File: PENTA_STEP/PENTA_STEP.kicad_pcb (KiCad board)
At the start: 4 copper layers, 200 x 100 mm, 364 parts, among them J1 DB25_Female_LCNC, J10 ENC_HEADER, J11 ENC_HEADER, J12 PSoC_PROG, J13 PWR_SW_CH1, J14 SCREW TERM, J15 SCREW TERM, J16 ENC_HEADER, J17 ENC_HEADER, J18 SCREW TERM, J19 SCREW TERM, J2 MTA-100, J20 CYP_I2C, J21 PWR_SW_CH2, J3 USB_B, J4 SPARE_IN, J5 ENC_HEADER, J6 Conn_02x02_Odd_Even, J7 CYP_GPIO, J8 ICSP, J9 SCREW TERM, Q1 BUK9K45-100E,115, Q10 BUK9K45-100E,115, Q11 BUK9K45-100E,115, Q12 BUK9K45-100E,115, Q13 BUK9K45-100E,115, Q14 BUK9K45-100E,115, Q15 BUK9K45-100E,115, Q16 BUK9K45-100E,115, Q17 BUK9K45-100E,115, Q18 BUK9K45-100E,115, Q19 BUK9K45-100E,115, Q2 BUK9K45-100E,115, Q20 BUK9K45-100E,115, Q21 AON7804, Q3 BUK9K45-100E,115, Q4 BUK9K45-100E,115, Q5 BUK9K45-100E,115, Q6 BUK9K45-100E,115, Q7 BUK9K45-100E,115, Q8 BUK9K45-100E,115, Q9 BUK9K45-100E,115, U1 ATTINY841-SSU, U2 CY8C5468AXI-LP106, U3 TMC5160-TA, U4 TMC5160-TA, U5 TMC5160-TA, U6 TMC5160-TA, U7 TMC5160-TA, Y1 10MHz

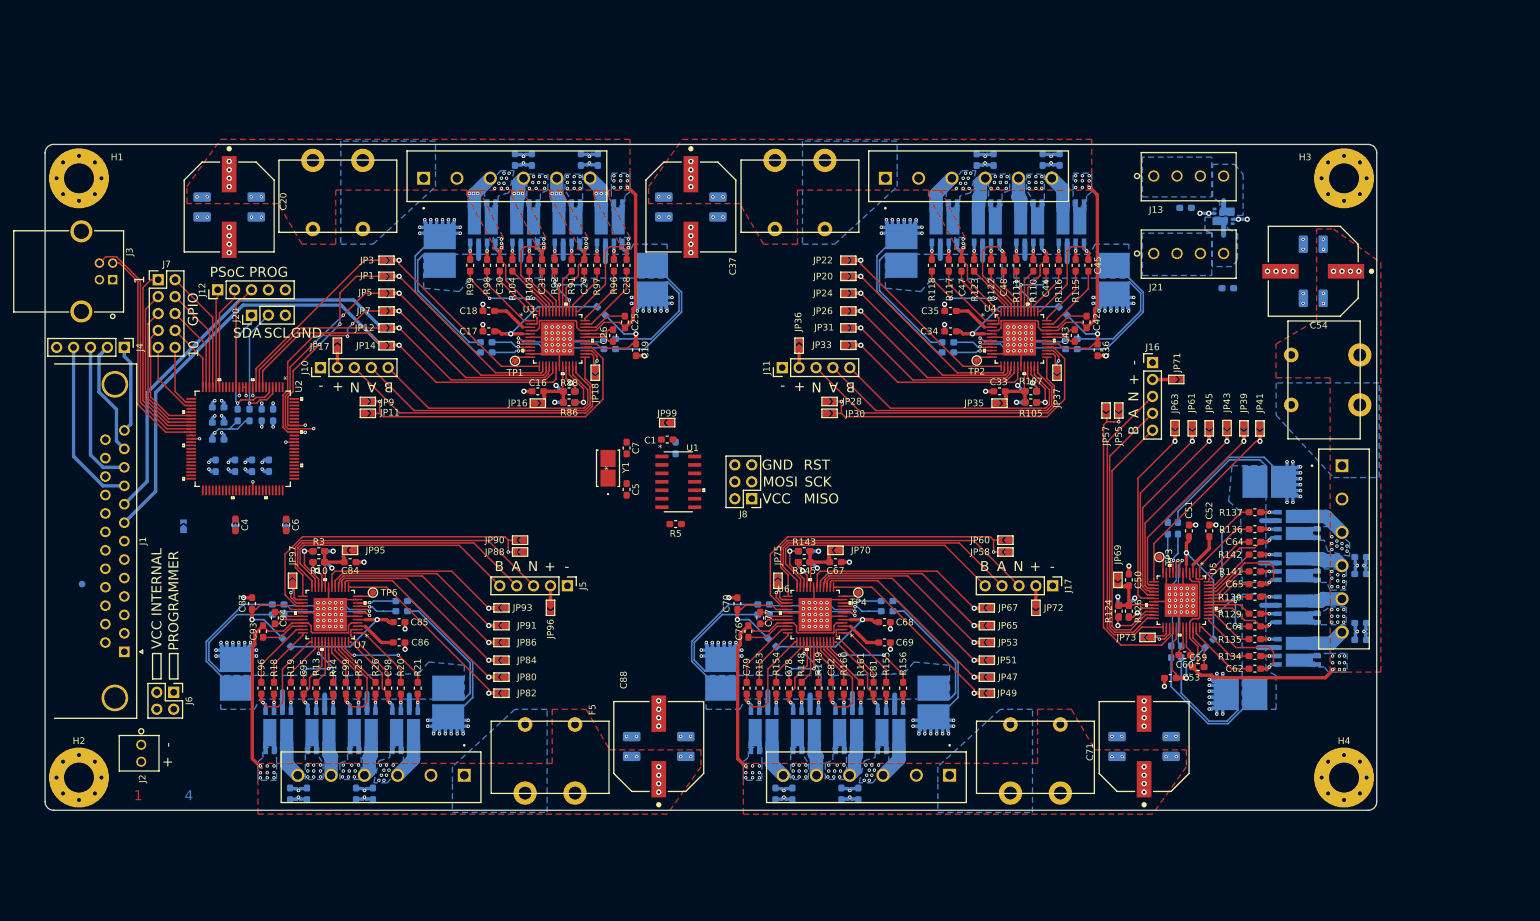
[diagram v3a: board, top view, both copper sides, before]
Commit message: majority routed, eliminated ATTINY coprocessor
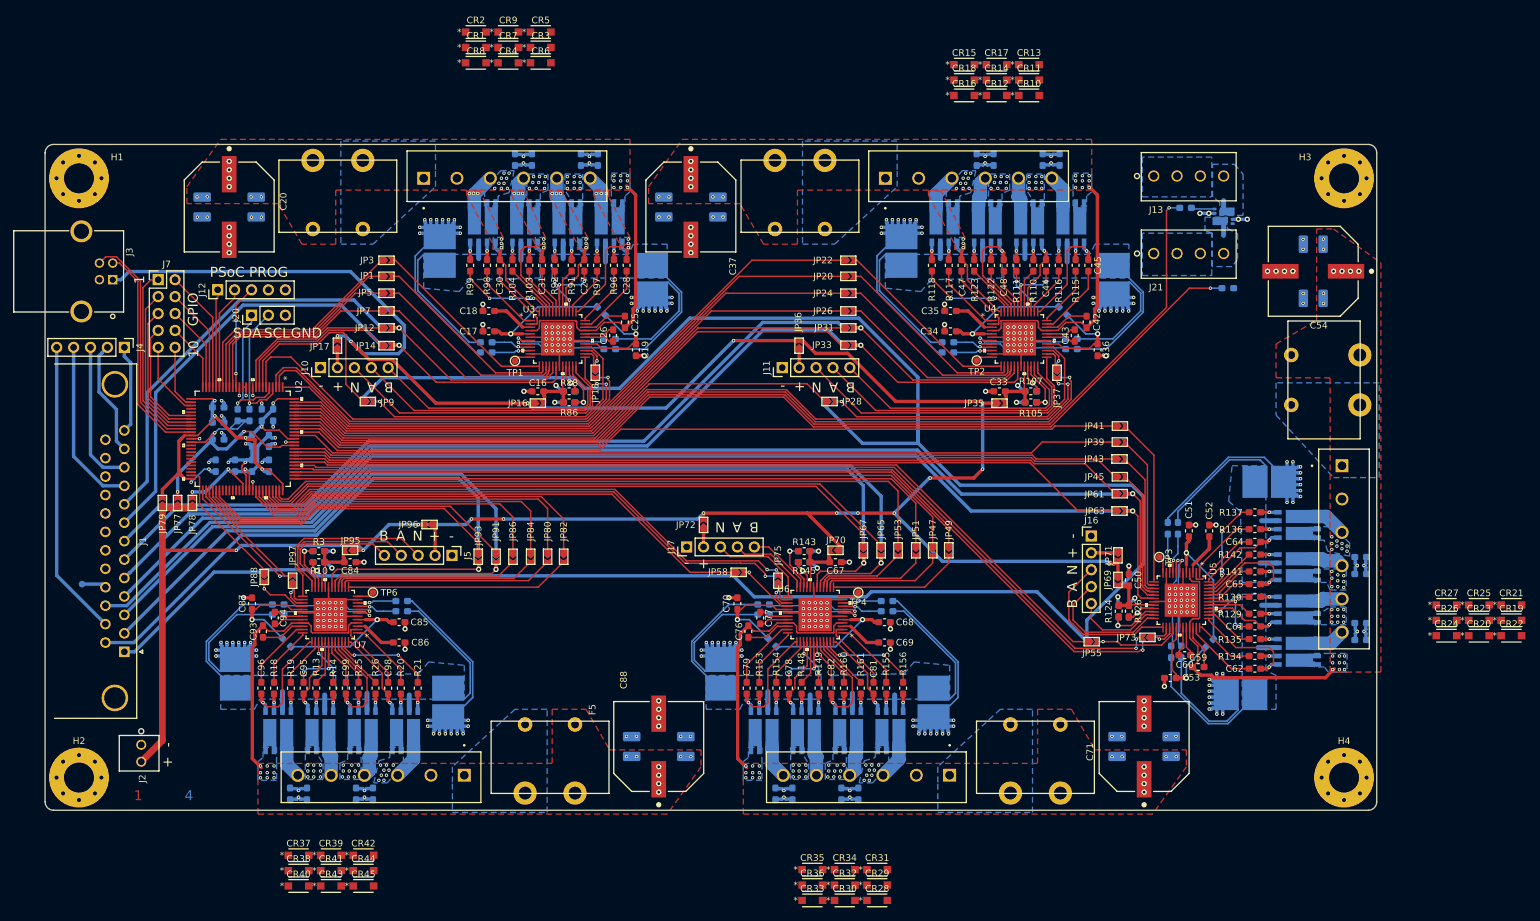
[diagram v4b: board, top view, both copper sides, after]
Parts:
- removed C1: 10u, Capacitor_SMD:C_0603_1608Metric_Pad1.05x0.95mm_HandSolder
- removed C2: 100n, Capacitor_SMD:C_0603_1608Metric_Pad1.05x0.95mm_HandSolder
- removed C5, C7: 18p, Capacitor_SMD:C_0603_1608Metric_Pad1.05x0.95mm_HandSolder
- removed J6: Conn_02x02_Odd_Even, Connector_PinHeader_2.54mm:PinHeader_2x02_P2.54mm_Vertical
- removed J8: ICSP, Connector_PinHeader_2.54mm:PinHeader_2x03_P2.54mm_Vertical
- removed JP10, JP2, JP21, JP23, JP25, JP27, JP29, JP4, JP40, JP42, JP44, JP46, JP48, JP50, JP52, JP54, JP56, JP59, JP6, JP8, JP81, JP83, JP85, JP87, JP89, JP99: SolderJumper_2_Open, CUSTOM_FP:small_triangle_jumper
- removed R5: 10k, Resistor_SMD:R_0603_1608Metric_Pad1.05x0.95mm_HandSolder
- removed U1: ATTINY841-SSU, CUSTOM_FP:ATTINY841-SSU
- removed Y1: 10MHz, CUSTOM_FP:CX5032GB10000H0PESZZ
- added CR1: PMEG6010CEGWX, CUSTOM_FP:PMEG6010CEGWX, F.Cu at (110.4, 35.0)
- added CR10: PMEG6010CEGWX, CUSTOM_FP:PMEG6010CEGWX, F.Cu at (193.5, 42.2)
- added CR11: PMEG6010CEGWX, CUSTOM_FP:PMEG6010CEGWX, F.Cu at (193.5, 39.9)
- added CR12: PMEG6010CEGWX, CUSTOM_FP:PMEG6010CEGWX, F.Cu at (188.6, 42.2)
- added CR13: PMEG6010CEGWX, CUSTOM_FP:PMEG6010CEGWX, F.Cu at (193.5, 37.5)
- added CR14: PMEG6010CEGWX, CUSTOM_FP:PMEG6010CEGWX, F.Cu at (188.6, 39.9)
- added CR15: PMEG6010CEGWX, CUSTOM_FP:PMEG6010CEGWX, F.Cu at (183.8, 37.5)
- added CR16: PMEG6010CEGWX, CUSTOM_FP:PMEG6010CEGWX, F.Cu at (183.8, 42.2)
- added CR17: PMEG6010CEGWX, CUSTOM_FP:PMEG6010CEGWX, F.Cu at (188.6, 37.5)
- added CR18: PMEG6010CEGWX, CUSTOM_FP:PMEG6010CEGWX, F.Cu at (183.8, 39.9)
- added CR19: PMEG6010CEGWX, CUSTOM_FP:PMEG6010CEGWX, F.Cu at (265.9, 121.0)
- added CR2: PMEG6010CEGWX, CUSTOM_FP:PMEG6010CEGWX, F.Cu at (110.4, 32.7)
- added CR20: PMEG6010CEGWX, CUSTOM_FP:PMEG6010CEGWX, F.Cu at (261.1, 123.3)
- added CR21: PMEG6010CEGWX, CUSTOM_FP:PMEG6010CEGWX, F.Cu at (265.9, 118.7)
- added CR22: PMEG6010CEGWX, CUSTOM_FP:PMEG6010CEGWX, F.Cu at (265.9, 123.3)
- added CR23: PMEG6010CEGWX, CUSTOM_FP:PMEG6010CEGWX, F.Cu at (261.1, 121.0)
- added CR24: PMEG6010CEGWX, CUSTOM_FP:PMEG6010CEGWX, F.Cu at (256.2, 123.3)
- added CR25: PMEG6010CEGWX, CUSTOM_FP:PMEG6010CEGWX, F.Cu at (261.1, 118.7)
- added CR26: PMEG6010CEGWX, CUSTOM_FP:PMEG6010CEGWX, F.Cu at (256.2, 121.0)
- added CR27: PMEG6010CEGWX, CUSTOM_FP:PMEG6010CEGWX, F.Cu at (256.2, 118.7)
- added CR28: PMEG6010CEGWX, CUSTOM_FP:PMEG6010CEGWX, F.Cu at (170.7, 163.1)
- added CR29: PMEG6010CEGWX, CUSTOM_FP:PMEG6010CEGWX, F.Cu at (170.7, 160.8)
- added CR3: PMEG6010CEGWX, CUSTOM_FP:PMEG6010CEGWX, F.Cu at (120.2, 35.0)
- added CR30: PMEG6010CEGWX, CUSTOM_FP:PMEG6010CEGWX, F.Cu at (165.8, 163.1)
- added CR31: PMEG6010CEGWX, CUSTOM_FP:PMEG6010CEGWX, F.Cu at (170.7, 158.5)
- added CR32: PMEG6010CEGWX, CUSTOM_FP:PMEG6010CEGWX, F.Cu at (165.8, 160.8)
- added CR33: PMEG6010CEGWX, CUSTOM_FP:PMEG6010CEGWX, F.Cu at (160.9, 163.1)
- added CR34: PMEG6010CEGWX, CUSTOM_FP:PMEG6010CEGWX, F.Cu at (165.8, 158.5)
- added CR35: PMEG6010CEGWX, CUSTOM_FP:PMEG6010CEGWX, F.Cu at (160.9, 158.5)
- added CR36: PMEG6010CEGWX, CUSTOM_FP:PMEG6010CEGWX, F.Cu at (160.9, 160.8)
- added CR37: PMEG6010CEGWX, CUSTOM_FP:PMEG6010CEGWX, F.Cu at (83.8, 156.3)
- added CR38: PMEG6010CEGWX, CUSTOM_FP:PMEG6010CEGWX, F.Cu at (83.8, 158.6)
- added CR39: PMEG6010CEGWX, CUSTOM_FP:PMEG6010CEGWX, F.Cu at (88.7, 156.3)
- added CR4: PMEG6010CEGWX, CUSTOM_FP:PMEG6010CEGWX, F.Cu at (115.3, 37.3)
- added CR40: PMEG6010CEGWX, CUSTOM_FP:PMEG6010CEGWX, F.Cu at (83.8, 160.9)
- added CR41: PMEG6010CEGWX, CUSTOM_FP:PMEG6010CEGWX, F.Cu at (88.7, 158.6)
- added CR42: PMEG6010CEGWX, CUSTOM_FP:PMEG6010CEGWX, F.Cu at (93.5, 156.3)
- added CR43: PMEG6010CEGWX, CUSTOM_FP:PMEG6010CEGWX, F.Cu at (88.7, 160.9)
- added CR44: PMEG6010CEGWX, CUSTOM_FP:PMEG6010CEGWX, F.Cu at (93.5, 158.6)
- added CR45: PMEG6010CEGWX, CUSTOM_FP:PMEG6010CEGWX, F.Cu at (93.5, 160.9)
- added CR5: PMEG6010CEGWX, CUSTOM_FP:PMEG6010CEGWX, F.Cu at (120.2, 32.7)
- added CR6: PMEG6010CEGWX, CUSTOM_FP:PMEG6010CEGWX, F.Cu at (120.2, 37.3)
- added CR7: PMEG6010CEGWX, CUSTOM_FP:PMEG6010CEGWX, F.Cu at (115.3, 35.0)
- added CR8: PMEG6010CEGWX, CUSTOM_FP:PMEG6010CEGWX, F.Cu at (110.4, 37.3)
- added CR9: PMEG6010CEGWX, CUSTOM_FP:PMEG6010CEGWX, F.Cu at (115.3, 32.7)
- C4, C6, JP11, JP30, JP57, JP60, JP90: moved to B.Cu
- JP77, JP78, JP79: moved to F.Cu
- moved J17 55.3 mm to (142.1, 110.0), turned to 90 degrees
- moved JP72 51.4 mm to (144.6, 106.7), turned to 90 degrees
- moved JP60 40.4 mm to (149.9, 113.8), turned to 0 degrees
- moved JP58 40.2 mm to (149.9, 113.8), turned to 0 degrees
- moved JP90 38.8 mm to (78.6, 114.5), turned to 270 degrees
- moved JP88 38.6 mm to (78.6, 114.5), turned to 270 degrees
- moved JP55 34.9 mm to (202.9, 124.2), turned to 0 degrees
- moved JP57 34.8 mm to (202.9, 124.2), turned to 0 degrees
- moved JP71 27.8 mm to (206.8, 111.3), turned to 270 degrees
- moved J16 27.6 mm to (202.8, 108.3)
- moved JP82 22.5 mm to (123.6, 111.5), turned to 270 degrees
- moved JP49 22.2 mm to (181.4, 110.5), turned to 270 degrees
- moved JP96 22.1 mm to (103.5, 106.6), turned to 180 degrees
- moved JP41 21.0 mm to (207.1, 91.8), turned to 0 degrees
- moved JP47 20.7 mm to (179.0, 110.5), turned to 270 degrees
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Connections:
- JP1 pad 1: /CYP_SCK -> /CYP_SCK1
- JP20 pad 1: /CYP_SCK -> /CYP_SCK2
- JP24 pad 1: /CYP_MOSI -> /CYP_MOSI2
- JP26 pad 1: /CYP_MISO -> /CYP_MISO2
- JP39 pad 1: /CYP_SCK -> /CYP_SCK3
- JP43 pad 1: /CYP_MOSI -> /CYP_MOSI3
- JP45 pad 1: /CYP_MISO -> /CYP_MISO3
- JP47 pad 1: /CYP_SCK -> /CYP_SCK4
- JP5 pad 1: /CYP_MOSI -> /CYP_MOSI1
- JP51 pad 1: /CYP_MOSI -> /CYP_MOSI4
- JP53 pad 1: /CYP_MISO -> /CYP_MISO4
- JP7 pad 1: /CYP_MISO -> /CYP_MISO1
- JP77 pad 1: Net-(J6-Pad2) -> /VCC_CONT
- JP78 pad 1: Net-(J6-Pad2) -> /VCC_CONT
- JP79 pad 1: Net-(J6-Pad2) -> /VCC_CONT
- JP80 pad 1: /CYP_SCK -> /CYP_SCK5
- JP84 pad 1: /CYP_MOSI -> /CYP_MOSI5
- JP86 pad 1: /CYP_MISO -> /CYP_MISO5
- U2 pad 1: Net-(U2-Pad1) -> /CYP_SCK2
- U2 pad 16: Net-(U2-Pad16) -> /CYP_MISO1
- U2 pad 17: Net-(U2-Pad17) -> /CYP_MOSI1
- U2 pad 18: Net-(U2-Pad18) -> /CYP_SCK1
- U2 pad 19: Net-(U2-Pad19) -> /CYP_CS1
- U2 pad 2: Net-(U2-Pad2) -> /CYP_CS2
- U2 pad 3: Net-(U2-Pad3) -> /DIAG_1_1
- U2 pad 44: /DIAG_1_5 -> Net-(U2-Pad44)
- U2 pad 45: /DIAG_0_5 -> Net-(U2-Pad45)
- U2 pad 46: /CYP_DIR5 -> Net-(U2-Pad46)
- U2 pad 47: /CYP_STEP5 -> Net-(U2-Pad47)
- U2 pad 48: /~CYP_ENA_5 -> Net-(U2-Pad48)
- U2 pad 49: /DIAG_1_4 -> /~CYP_ENA_5
- U2 pad 51: /DIAG_0_4 -> /DIAG_1_5
- U2 pad 52: /CYP_DIR4 -> /DIAG_0_5
- U2 pad 53: Net-(U2-Pad53) -> /CYP_DIR5
- U2 pad 54: Net-(U2-Pad54) -> /CYP_STEP5
- U2 pad 55: Net-(U2-Pad55) -> /CYP_MISO5
- U2 pad 56: Net-(U2-Pad56) -> /CYP_MOSI5
- U2 pad 6: Net-(U2-Pad6) -> /DIAG_0_1
- U2 pad 67: Net-(U2-Pad67) -> /CYP_SCK5
- U2 pad 68: Net-(U2-Pad68) -> /CYP_CS5
- U2 pad 69: /CYP_STEP4 -> /~CYP_ENA_4
- U2 pad 7: /CYP_DIR1 -> /~CYP_ENA_1
- U2 pad 70: /~CYP_ENA_4 -> /DIAG_1_4
- U2 pad 71: /DIAG_1_3 -> /DIAG_0_4
- U2 pad 72: /DIAG_0_3 -> /CYP_DIR4
- U2 pad 73: /CYP_DIR3 -> /CYP_STEP4
- U2 pad 74: /CYP_STEP3 -> /CYP_MISO4
- U2 pad 76: /~CYP_ENA_3 -> /CYP_MOSI4
- U2 pad 77: /DIAG_1_2 -> /CYP_SCK4
- U2 pad 78: /DIAG_0_2 -> /CYP_CS4
- U2 pad 79: /CYP_DIR2 -> /DIAG_1_3
- U2 pad 8: /CYP_STEP1 -> /CYP_DIR1
- U2 pad 80: /CYP_STEP2 -> /DIAG_0_3
- U2 pad 81: /~CYP_ENA_2 -> /~CYP_ENA_3
- U2 pad 82: /DIAG_1_1 -> /CYP_DIR3
- U2 pad 83: /DIAG_0_1 -> /CYP_STEP3
- U2 pad 84: /PWR_SW_CH2 -> /CYP_MISO3
- U2 pad 85: /PWR_SW_CH1 -> /CYP_MOSI3
- U2 pad 89: /~CYP_ENA_1 -> /CYP_SCK3
- U2 pad 9: /CYP_CS1 -> /CYP_STEP1
- U2 pad 90: /CYP_MISO -> /CYP_CS3
- U2 pad 91: /CYP_MOSI -> /PWR_SW_CH2
- U2 pad 92: /CYP_SCK -> /PWR_SW_CH1
- U2 pad 93: Net-(U2-Pad93) -> /DIAG_1_2
- U2 pad 94: Net-(U2-Pad94) -> /DIAG_0_2
- U2 pad 95: /CYP_CS5 -> /~CYP_ENA_2
- U2 pad 96: /CYP_CS4 -> /CYP_DIR2
- U2 pad 97: /CYP_CS3 -> /CYP_STEP2
- U2 pad 98: /CYP_CS2 -> /CYP_MISO2
- U2 pad 99: Net-(U2-Pad99) -> /CYP_MOSI2
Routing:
- net /VCC_CONT: track 0.00 -> 405.8 mm, vias 0 -> 17
- net /~PAR_ENA: track 0.00 -> 343.2 mm
- net /PWR_SW_CH1: track 0.00 -> 161.2 mm, vias 0 -> 1
- net /PAR_DIR3: track 0.00 -> 161.0 mm
- net /PAR_STEP3: track 0.00 -> 159.5 mm
- net /PWR_SW_CH2: track 0.00 -> 154.1 mm, vias 0 -> 1
- net /DIAG_1_3: track 0.00 -> 140.8 mm, vias 0 -> 1
- net /DIAG_0_3: track 0.00 -> 140.2 mm, vias 0 -> 2
- net /PAR_STEP4: track 0.00 -> 134.5 mm
- net /~CYP_ENA_3: track 0.00 -> 130.2 mm
- net /PAR_DIR4: track 0.00 -> 130.0 mm
- net /DIAG_1_2: track 0.00 -> 129.6 mm, vias 0 -> 1
- net /DIAG_0_2: track 0.00 -> 128.5 mm, vias 0 -> 2
- net /CYP_DIR3: track 0.00 -> 126.5 mm
- net /CYP_CS3: track 0.00 -> 125.9 mm
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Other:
- board text removed: "MISO"
- board text removed: "MOSI"
- board text removed: "PROGRAMMER"
- board text removed: "SCK"
- board text removed: "VCC"
- board text removed: "VCC INTERNAL"

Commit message: completed preliminary routing, still need plane touchup
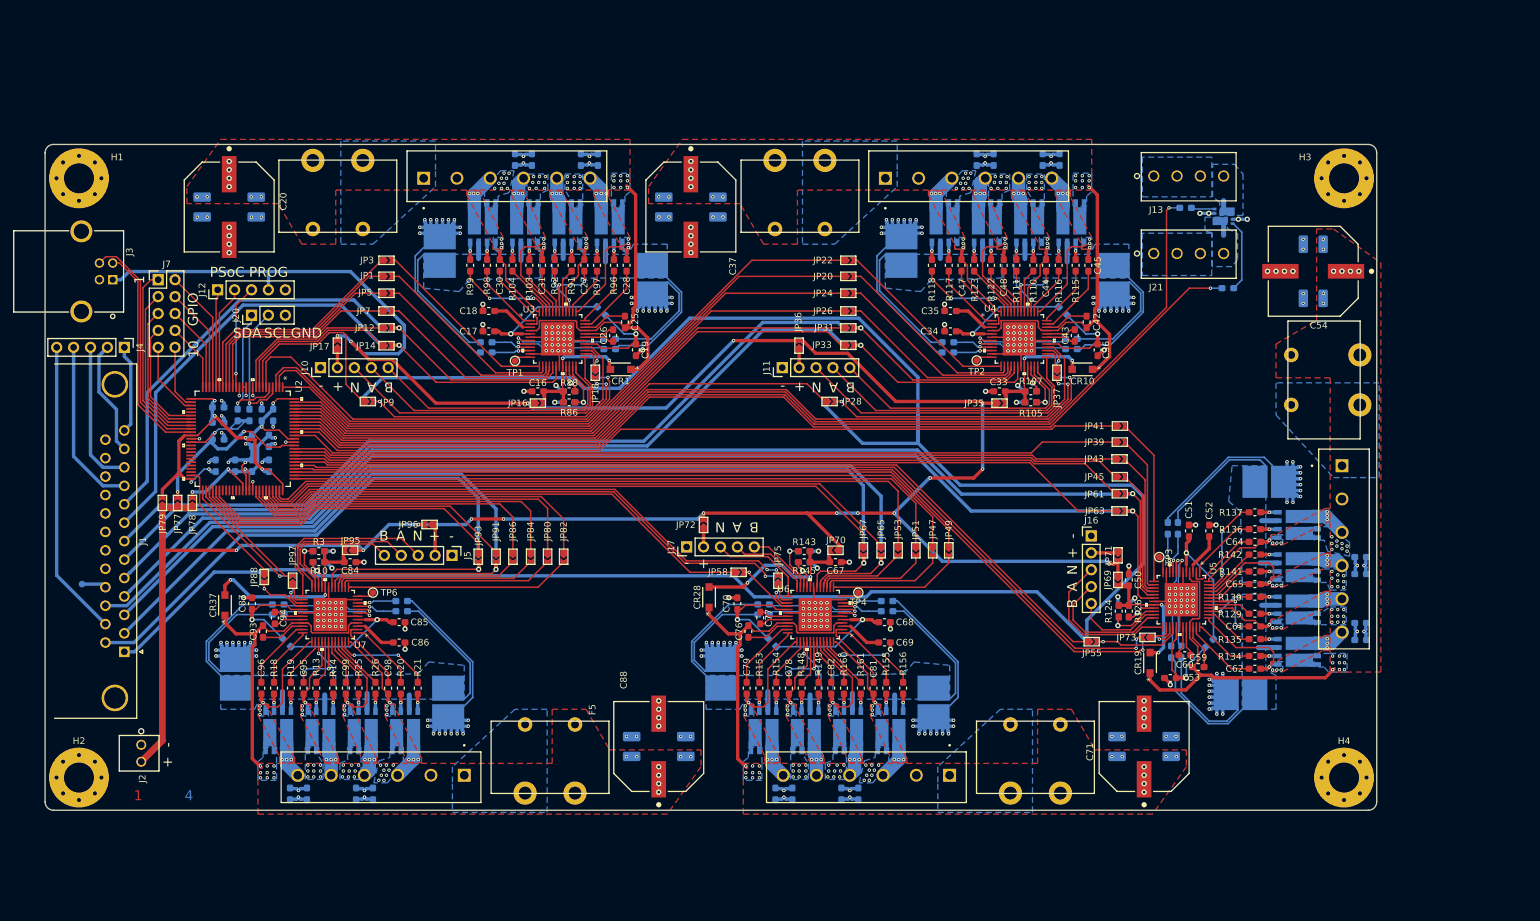
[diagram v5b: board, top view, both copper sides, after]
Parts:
- removed CR11, CR12, CR13, CR14, CR15, CR16, CR17, CR18, CR2, CR20, CR21, CR22, CR23, CR24, CR25, CR26, CR27, CR29, CR3, CR30, CR31, CR32, CR33, CR34, CR35, CR36, CR38, CR39, CR4, CR40, CR41, CR42, CR43, CR44, CR45, CR5, CR6, CR7, CR8, CR9: PMEG6010CEGWX, CUSTOM_FP:PMEG6010CEGWX
- moved CR19 54.6 mm to (211.7, 127.4), turned to 90 degrees
- moved CR1 53.0 mm to (132.2, 83.3), turned to 180 degrees
- moved CR28 52.1 mm to (145.4, 117.5), turned to 90 degrees
- moved CR10 41.9 mm to (201.5, 83.3), turned to 180 degrees
- moved CR37 39.1 mm to (72.7, 118.7), turned to 90 degrees
- moved U5 0.08 mm to (216.4, 117.9)
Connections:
- J12 pad 4: /VTARG -> /VCC_CONT
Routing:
- net /DRIVE_5/VCC_IO: track 10.5 -> 29.7 mm, vias 0 -> 2
- net /DRIVE_4/VCC_IO: track 10.5 -> 27.9 mm, vias 0 -> 2
- net Net-(Q21-PadG2): track 0.00 -> 10.8 mm
- net /DRIVE_1/VM: track 45.5 -> 55.9 mm
- net /DRIVE_3/VM: track 45.5 -> 55.7 mm
- net /DRIVE_3/VCC_IO: track 10.5 -> 20.6 mm, vias 0 -> 2
- net /DRIVE_2/VCC_IO: track 10.5 -> 20.6 mm, vias 0 -> 2
- net /DRIVE_1/VCC_IO: track 10.5 -> 20.5 mm, vias 0 -> 2
- net /DRIVE_2/VM: track 45.5 -> 55.3 mm
- net /DRIVE_4/VM: track 45.5 -> 52.4 mm
- net /DRIVE_5/VM: track 45.5 -> 51.7 mm
- net /VCC_CONT: track 405.8 -> 408.6 mm
- net /DRIVE_2/BMB1: track 19.1 -> 17.8 mm, vias 3 -> 6
- net /DRIVE_2/BMA1: track 15.9 -> 14.9 mm, vias 1 -> 6
- net /DRIVE_2/BMB2: track 21.7 -> 20.9 mm, vias 1 -> 6
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- added copper zone on B.Cu, net /DRIVE_2/BMA1
- added copper zone on F.Cu, net /DRIVE_2/BMA1
- added copper zone on B.Cu, net /DRIVE_2/BMA2
- added copper zone on F.Cu, net /DRIVE_2/BMA2
- added copper zone on F.Cu, net /DRIVE_2/BMB1
- added copper zone on B.Cu, net /DRIVE_2/BMB2
- added copper zone on F.Cu, net /DRIVE_2/BMB2
- added copper zone on B.Cu, net /DRIVE_3/BMA1
- added copper zone on F.Cu, net /DRIVE_3/BMA1
- added copper zone on B.Cu, net /DRIVE_3/BMA2
- added copper zone on F.Cu, net /DRIVE_3/BMA2
- added copper zone on B.Cu, net /DRIVE_3/BMB1
- added copper zone on F.Cu, net /DRIVE_3/BMB1
- added copper zone on B.Cu, net /DRIVE_3/BMB2
- added copper zone on F.Cu, net /DRIVE_3/BMB2
- added copper zone on B.Cu, net /DRIVE_4/BMA1
- added copper zone on F.Cu, net /DRIVE_4/BMA1
- added copper zone on B.Cu, net /DRIVE_4/BMA2
- added copper zone on F.Cu, net /DRIVE_4/BMA2
- added copper zone on B.Cu, net /DRIVE_4/BMB1
- added copper zone on F.Cu, net /DRIVE_4/BMB1
- added copper zone on B.Cu, net /DRIVE_4/BMB2
- added copper zone on F.Cu, net /DRIVE_4/BMB2
- added copper zone on B.Cu, net /DRIVE_5/BMA1
- added copper zone on F.Cu, net /DRIVE_5/BMA1
- added copper zone on B.Cu, net /DRIVE_5/BMA2
- added copper zone on F.Cu, net /DRIVE_5/BMA2
- added copper zone on B.Cu, net /DRIVE_5/BMB1
- added copper zone on F.Cu, net /DRIVE_5/BMB1
- added copper zone on B.Cu, net /DRIVE_5/BMB2
- added copper zone on F.Cu, net /DRIVE_5/BMB2
